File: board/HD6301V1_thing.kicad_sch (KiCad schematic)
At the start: 32 parts, among them J1 Conn_01x02_Male, J2 8bit_thing_bus_connector, J3 P1_connector, J4 P2_conn, SW1 Reset, SW2 SW_DIP_x02, U1 APX811-46, U2 CD4053B, U3 HD6301V1, U4 SLG46826G, U5 74HCT573, U6 IS62C256AL, U7 SST39SF010, X1 CXO_DIP14

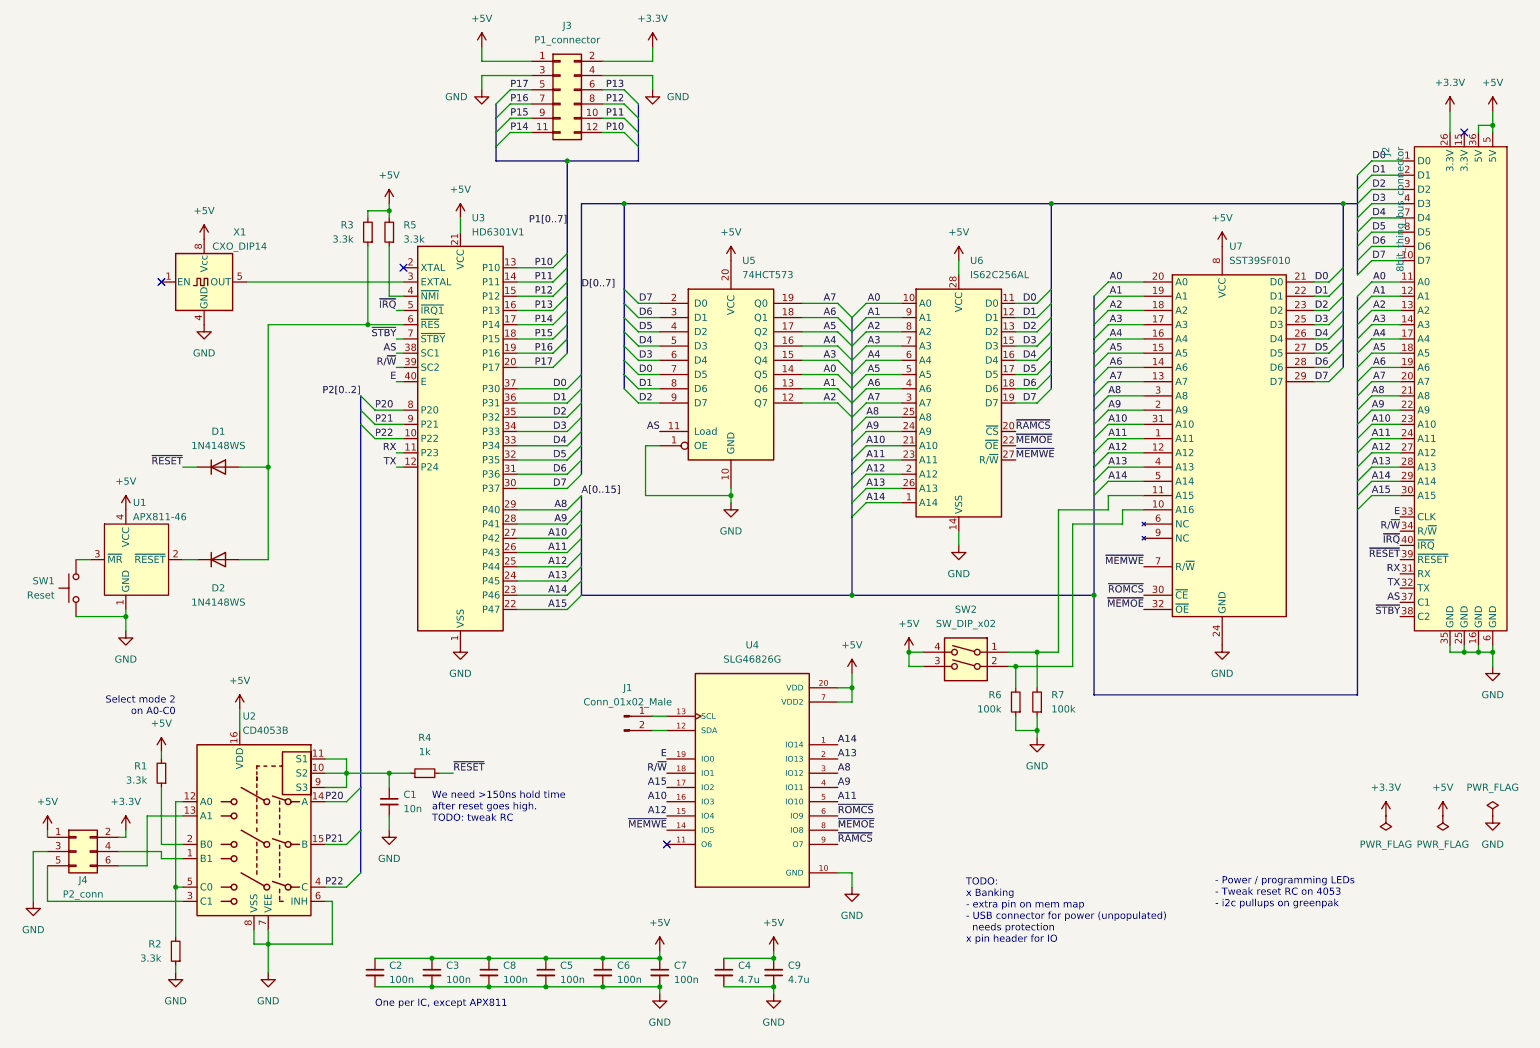
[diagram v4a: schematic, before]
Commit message: Finished HD6301 board
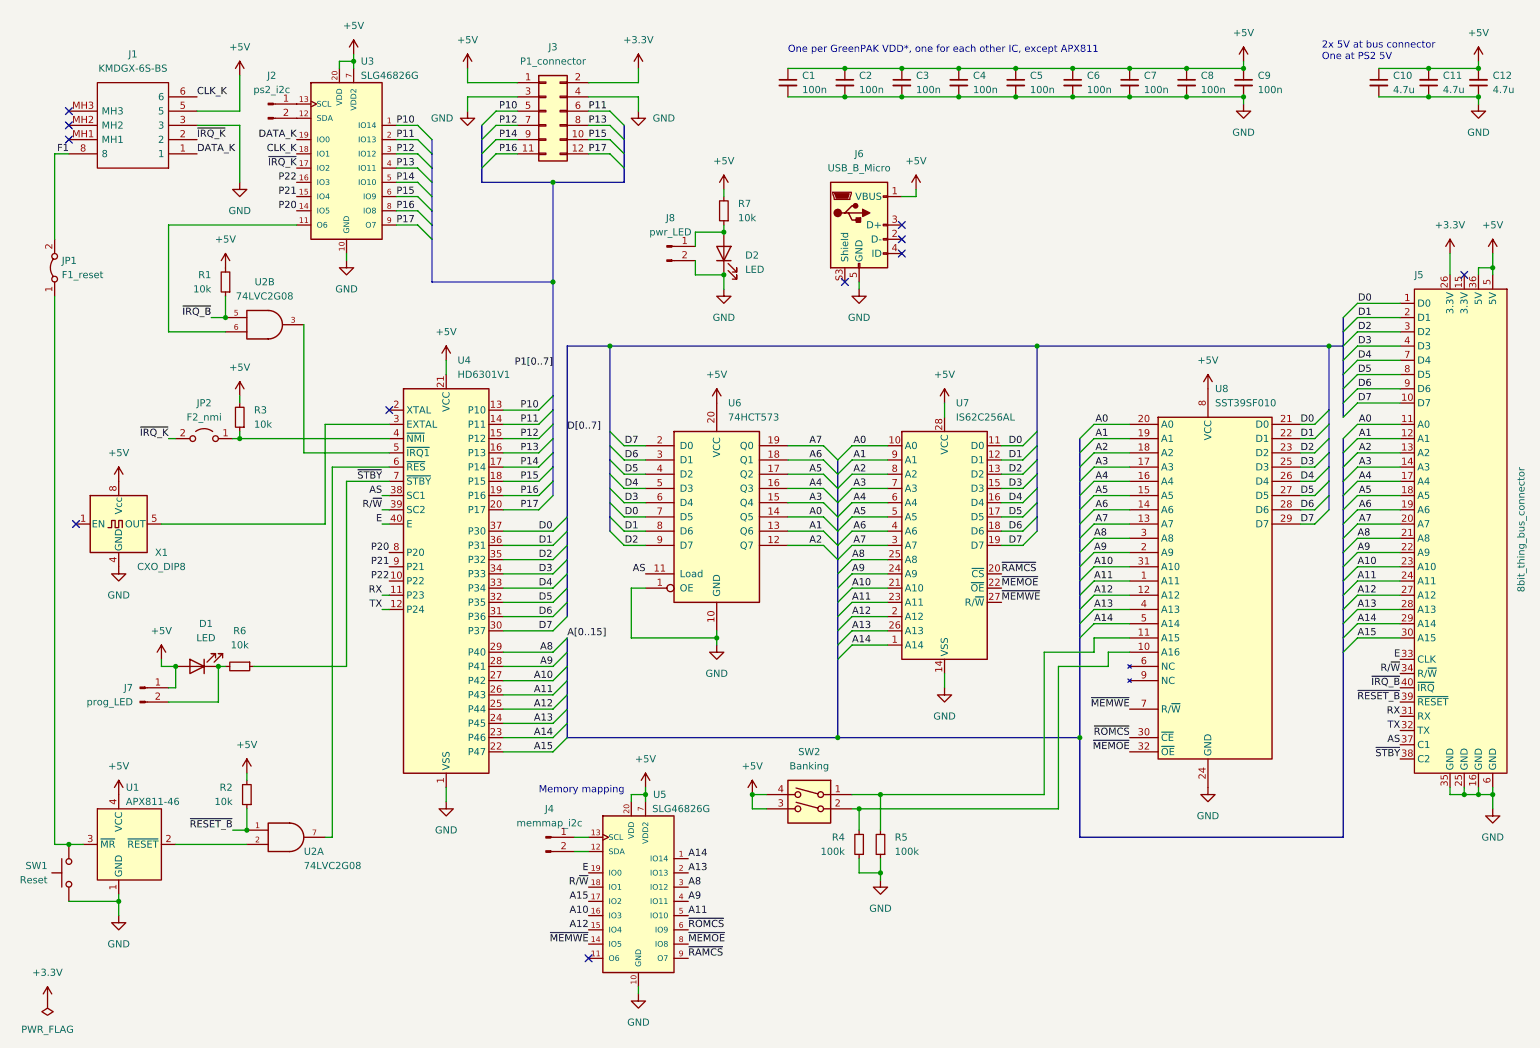
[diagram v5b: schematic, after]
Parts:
- removed C1: 10n, Capacitor_SMD:C_0805_2012Metric_Pad1.18x1.45mm_HandSolder, symbol Device:C_Small
- removed D1, D2: 1N4148WS, Diode_SMD:D_SOD-323, symbol Diode:1N4148WS
- removed J4: P2_conn, Connector_PinHeader_2.54mm:PinHeader_2x03_P2.54mm_Horizontal, symbol Connector_Generic:Conn_02x03_Odd_Even
- removed R2: 3.3k, Resistor_SMD:R_0805_2012Metric_Pad1.20x1.40mm_HandSolder, symbol Device:R_Small
- removed R4: 1k, Resistor_SMD:R_0805_2012Metric_Pad1.20x1.40mm_HandSolder, symbol Device:R_Small
- removed U2: CD4053B, Package_SO:SOIC-16_3.9x9.9mm_P1.27mm, symbol Analog_Switch:CD4053B
- added C12: 4.7u, Capacitor_SMD:C_0805_2012Metric_Pad1.18x1.45mm_HandSolder, symbol Device:C_Small
- added C7, C8, C9: 100n, Capacitor_SMD:C_0805_2012Metric_Pad1.18x1.45mm_HandSolder, symbol Device:C_Small
- added D1, D2: LED, LED_SMD:LED_0805_2012Metric_Pad1.15x1.40mm_HandSolder, symbol Device:LED
- added J1: KMDGX-6S-BS, imported_footprints:KMDGX6SBS, symbol imported_symbols:KMDGX-6S-BS
- added J2: ps2_i2c, Connector_PinHeader_2.54mm:PinHeader_1x02_P2.54mm_Vertical, symbol Connector:Conn_01x02_Male
- added J6: USB_B_Micro, imported_footprints:AMPHENOL_10118194-0001LF_MICRO_USB_improved, symbol own_symbols:USB_B_Micro_with_shield_pins
- added J7: prog_LED, own_footprints:PinHeader_1x02_P2.54mm_Vertical_minimal, symbol Connector:Conn_01x02_Male
- added J8: pwr_LED, own_footprints:PinHeader_1x02_P2.54mm_Vertical_minimal, symbol Connector:Conn_01x02_Male
- added JP1: F1_reset, Connector_PinHeader_2.54mm:PinHeader_1x02_P2.54mm_Vertical, symbol Jumper:Jumper_2_Bridged
- added JP2: F2_nmi, Connector_PinHeader_2.54mm:PinHeader_1x02_P2.54mm_Vertical, symbol Jumper:Jumper_2_Open
- added R6, R7: 10k, Resistor_SMD:R_0805_2012Metric_Pad1.20x1.40mm_HandSolder, symbol Device:R_Small
- added U2: 74LVC2G08, Package_SO:VSSOP-8_2.3x2mm_P0.5mm, symbol own_symbols:74LVC2G08_5V_power
- added U3: SLG46826G, imported_footprints:SOP65P640X120-20N, symbol imported_symbols:SLG46826G
- J4: renamed from J1; value Conn_01x02_Male -> memmap_i2c
- R1: value 3.3k -> 10k
- R2: renamed from R3; value 3.3k -> 10k
- R3: renamed from R5; value 3.3k -> 10k
- SW2: value SW_DIP_x02 -> Banking
- U5: renamed from U4; footprint Package_SO:TSSOP-20_4.4x6.5mm_P0.65mm -> imported_footprints:SOP65P640X120-20N
- X1: value CXO_DIP14 -> CXO_DIP8
- renumbered C2 to C1, C4 to C10, C9 to C11, C3 to C2, C8 to C3, C5 to C4, C6 to C5, C7 to C6, J2 to J5, R6 to R4, R7 to R5, U3 to U4, U5 to U6, U6 to U7, U7 to U8
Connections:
- net +5V: now also C12.2, C7.1, C8.1, C9.1, D1.2 (A), J1.5, J6.1 (VBUS), J7.1 (Pin_1), R7.2, U2.8 (+5V), U2.8 (+5V), U3.20 (VDD), U3.7 (VDD2)
- net GND: now also C12.1, C7.2, C8.2, C9.2, D2.1 (K), J1.3, J6.5 (GND), J8.2 (Pin_2), U2.4 (GND), U2.4 (GND), U3.10 (GND)
- net P10: now also J3.5 (Pin_5), U3.1 (IO14); no longer J3.12 (Pin_12)
- net P11: now also J3.6 (Pin_6), U3.2 (IO13); no longer J3.10 (Pin_10)
- net P12: now also J3.7 (Pin_7), U3.3 (IO12); no longer J3.8 (Pin_8)
- net P13: now also J3.8 (Pin_8), U3.4 (IO11); no longer J3.6 (Pin_6)
- net P14: now also J3.9 (Pin_9), U3.5 (IO10); no longer J3.11 (Pin_11)
- net P15: now also J3.10 (Pin_10), U3.6 (IO9); no longer J3.9 (Pin_9)
- net P16: now also J3.11 (Pin_11), U3.8 (IO8); no longer J3.7 (Pin_7)
- net P17: now also J3.12 (Pin_12), U3.9 (O7); no longer J3.5 (Pin_5)
- net P20: now also U3.14 (IO5)
- net P21: now also U3.15 (IO4)
- net P22: now also U3.16 (IO3)
- net ~{STBY}: now also R6.1
- net at U1.2 (~{RESET}): now also U2.2
- net at U4.6 (~{RES}): now also U2.7; no longer R2.1
- net at SW1.2, U1.3 (~{MR}): now also JP1.1 (A)
- net ~{IRQ_B}: now reaches R1.1
- net ~{IRQ_B}: now also J5.40 (~{IRQ}), U2.5
- net at R3.1, U4.4 (~{NMI}): now also JP2.1 (A)
- net ~{IRQ}: no longer names the net of U4.5 (~{IRQ1})
- net ~{IRQ}: now also U2.3; no longer J5.40 (~{IRQ})
- net ~{RESET} renamed ~{RESET_B}
- net ~{RESET_B}: now also R2.1, U2.1
- new net: U2.6, U3.11 (O6)
- new net: D2.2 (A), J8.1 (Pin_1), R7.1
- new net: J2.2 (Pin_2), U3.12 (SDA)
- new net: J2.1 (Pin_1), U3.13 (SCL)
- new net: D1.1 (K), J7.2 (Pin_2), R6.2
- new net CLK_K: J1.6, U3.18 (IO1)
- new net DATA_K: J1.1, U3.19 (IO0)
- new net F1: J1.8, JP1.2 (B)
- new net ~{IRQ_K}: J1.2, JP2.2 (B), U3.17 (IO2)
- no-connect marks 4 -> 11
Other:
- note added: "2x 5V at bus connector One at PS2 5V"
- note added: "Memory mapping"
- note added: "One per GreenPAK VDD*, one for each other IC, except APX811"
- note removed: "- Power / programming LEDs - Tweak reset RC on 4053 - i2c pullups on greenpak"
- note removed: "One per IC, except APX811"
- note removed: "Select mode 2 on A0-C0"
- note removed: "TODO: x Banking - extra pin on mem map - USB connector for power (unpopulated) needs protection x pin header for IO"
- note removed: "We need >150ns hold time after reset goes high. TODO: tweak RC"
- moved on the sheet: C1, C10, C11, C2, C3, C4, C5, C6, J3, J4, J5, R2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

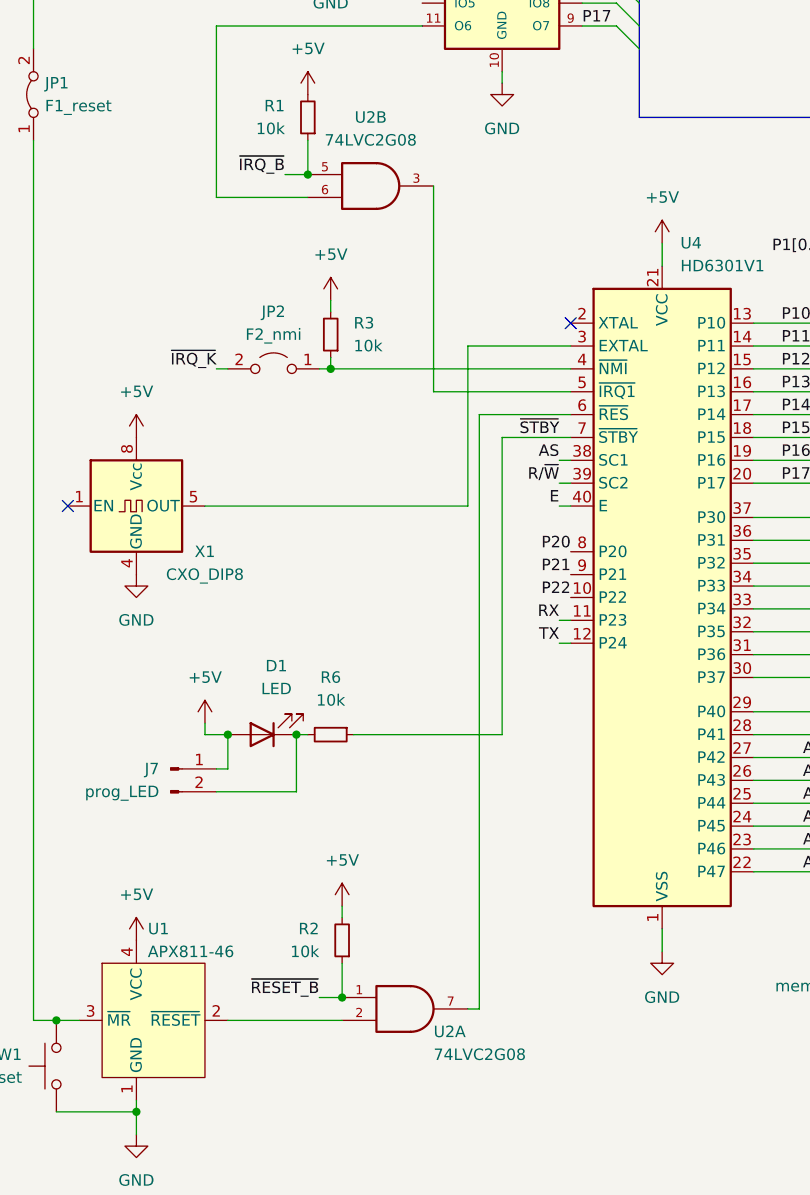
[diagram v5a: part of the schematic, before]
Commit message: Update board files to Kicad 7.0
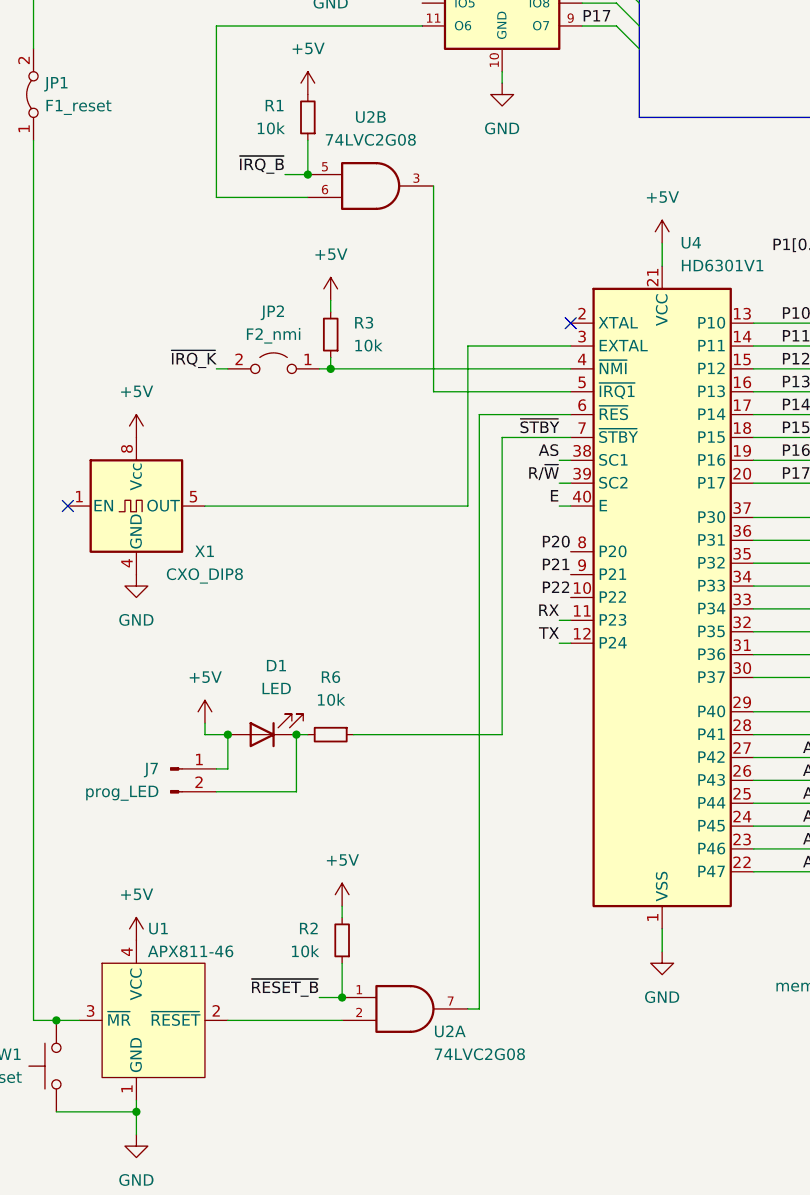
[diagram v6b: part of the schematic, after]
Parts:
- J2, J4, J7, J8: symbol Connector:Conn_01x02_Male -> Connector:Conn_01x02_Pin
- J3: footprint Connector_PinHeader_2.54mm:PinHeader_2x06_P2.54mm_Horizontal -> own_footprints:PinHeader_2x06_P2.54mm_Horizontal_no_graphics
- JP1, JP2: footprint Connector_PinHeader_2.54mm:PinHeader_1x02_P2.54mm_Vertical -> own_footprints:PinHeader_1x02_P2.54mm_Vertical_minimal
